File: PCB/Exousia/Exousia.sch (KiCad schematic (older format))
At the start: 74 parts, among them J1 IN/out, J2 I2C buss, J3 in/OUT, Q1 2N7002, Q2 2N7002, Q3 2N7002, U1 AON7410, U2 AON7410, U3 RVSPG, U4 AON7410, U5 AON7410

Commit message: did work
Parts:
- removed J1: IN/out, Connector_PinSocket_2.54mm:PinSocket_1x04_P2.54mm_Vertical, symbol Connector:Conn_01x02_Female
- removed J3: in/OUT, Connector_PinSocket_2.54mm:PinSocket_1x02_P2.54mm_Vertical, symbol Connector:Conn_01x02_Female
- removed TP1: RVSPG, TestPoint:TestPoint_Loop_D2.50mm_Drill1.0mm, symbol Connector:TestPoint
- removed TP2: FRWPG, TestPoint:TestPoint_Loop_D2.50mm_Drill1.0mm, symbol Connector:TestPoint
- added J1: IN/out, Connector_PinSocket_2.54mm:PinSocket_1x04_P2.54mm_Vertical, symbol Connector:Conn_01x04_Female
- added J3: in/OUT, Connector_PinSocket_2.54mm:PinSocket_1x04_P2.54mm_Vertical, symbol Connector:Conn_01x04_Female
- D1, D3: value LED -> FRWPG
- D4: value LED -> RVSPG
- JP1: value SolderJumper_3_Open -> IO-Vselect; footprint Connector_PinSocket_2.54mm:PinSocket_1x03_P2.54mm_Vertical -> Jumper:SolderJumper-3_P1.3mm_Open_RoundedPad1.0x1.5mm_NumberLabels
- JP2: value SolderJumper_3_Open -> Pin_FRWEN / ADP; footprint Connector_PinSocket_2.54mm:PinSocket_1x03_P2.54mm_Vertical -> Jumper:SolderJumper-3_P1.3mm_Open_RoundedPad1.0x1.5mm_NumberLabels
- JP3: value SolderJumper_3_Open -> RVSEN; footprint Connector_PinSocket_2.54mm:PinSocket_1x03_P2.54mm_Vertical -> Jumper:SolderJumper-3_P1.3mm_Open_RoundedPad1.0x1.5mm_NumberLabels
- JP4: value SolderJumper_3_Open -> Pin_FRWEN; footprint Connector_PinSocket_2.54mm:PinSocket_1x03_P2.54mm_Vertical -> Jumper:SolderJumper-3_P1.3mm_Open_RoundedPad1.0x1.5mm_NumberLabels
- L1: footprint (none) -> Inductor_SMD:L_6.3x6.3_H3
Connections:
- net GND: now also J1.1 (Pin_1), J1.2 (Pin_2), J3.1 (Pin_1), J3.2 (Pin_2)
- net at D2.1, R1.2, R2.2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: now also J1.3 (Pin_3), J1.4 (Pin_4)
- net at R24.1, R25.2: now also J3.3 (Pin_3), J3.4 (Pin_4)
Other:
- note added: "change component values for 12A system, \n- inductor\n- mosfets\n- sense resistors\nchange footprint for IC\nmake footprint for inductor"
- note removed: "find foot prints of all passives \n\n"
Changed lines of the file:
@@
 $EndDescr
-$Comp
-L Connector:Conn_01x02_Female J1
-U 1 1 5FC12546
-P 1750 1650
-F 0 "J1" H 1642 1325 50  0000 C CNN
-F 1 "IN/out" H 1642 1416 50  0000 C CNN
-F 2 "Connector_PinSocket_2.54mm:PinSocket_1x04_P2.54mm_Vertical" H 1750 1650 50  0001 C CNN
-F 3 "~" H 1750 1650 50  0001 C CNN
-	1    1750 1650
-	-1   0    0    1
-$EndComp
-$Comp
-L Connector:Conn_01x02_Female J3
-U 1 1 5FC12995
-P 13450 1650
-F 0 "J3" H 13478 1626 50  0000 L CNN
-F 1 "in/OUT" H 13478 1535 50  0000 L CNN
-F 2 "Connector_PinSocket_2.54mm:PinSocket_1x02_P2.54mm_Vertical" H 13450 1650 50  0001 C CNN
-F 3 "~" H 13450 1650 50  0001 C CNN
-	1    13450 1650
-	1    0    0    1
-$EndComp
 $Comp
 L ISL95338:ISL95338 U3
@@
 F 0 "L1" V 7840 2050 50  0000 C CNN
 F 1 "2uH" V 7749 2050 50  0000 C CNN
-F 2 "" H 7650 2050 50  0001 C CNN
+F 2 "Inductor_SMD:L_6.3x6.3_H3" H 7650 2050 50  0001 C CNN
 F 3 "~" H 7650 2050 50  0001 C CNN
 	1    7650 2050
@@
 L power:GND #PWR0105
 U 1 1 5FC5C5A0
-P 2000 1750
-F 0 "#PWR0105" H 2000 1500 50  0001 C CNN
-F 1 "GND" H 2005 1577 50  0000 C CNN
-F 2 "" H 2000 1750 50  0001 C CNN
-F 3 "" H 2000 1750 50  0001 C CNN
-	1    2000 1750
+P 2000 1850
+F 0 "#PWR0105" H 2000 1600 50  0001 C CNN
+F 1 "GND" H 2005 1677 50  0000 C CNN
+F 2 "" H 2000 1850 50  0001 C CNN
+F 3 "" H 2000 1850 50  0001 C CNN
+	1    2000 1850
 	1    0    0    -1
 $EndComp
@@
 Wire Wire Line
 	10000 5100 10000 4950
-$Comp
-L Connector:TestPoint TP2
-U 1 1 5FD06A05
-P 9300 4800
-F 0 "TP2" H 9358 4918 50  0000 L CNN
-F 1 "FRWPG" H 9358 4827 50  0000 L CNN
-F 2 "TestPoint:TestPoint_Loop_D2.50mm_Drill1.0mm" H 9500 4800 50  0001 C CNN
-F 3 "~" H 9500 4800 50  0001 C CNN
-	1    9300 4800
-	1    0    0    -1
-$EndComp
-Wire Wire Line
-	8900 5000 9300 5000
-Wire Wire Line
-	8800 5100 8950 5100
-Wire Wire Line
-	9300 4800 9300 5000
-$Comp
-L Connector:TestPoint TP1
-U 1 1 5FD1FD32
-P 8950 4800
-F 0 "TP1" H 9008 4918 50  0000 L CNN
-F 1 "RVSPG" H 9008 4827 50  0000 L CNN
-F 2 "TestPoint:TestPoint_Loop_D2.50mm_Drill1.0mm" H 9150 4800 50  0001 C CNN
-F 3 "~" H 9150 4800 50  0001 C CNN
-	1    8950 4800
-	1    0    0    -1
-$EndComp
-Wire Wire Line
-	8950 4800 8950 5100
-Connection ~ 8950 5100
-Connection ~ 9300 5000
-Wire Wire Line
-	9300 5000 9650 5000
-Wire Wire Line
-	8950 5100 10000 5100
 Wire Wire Line
 	8900 5000 8900 4550
@@
 L power:GND #PWR0110
 U 1 1 5FD5060D
-P 13200 1700
-F 0 "#PWR0110" H 13200 1450 50  0001 C CNN
-F 1 "GND" H 13205 1527 50  0000 C CNN
-F 2 "" H 13200 1700 50  0001 C CNN
-F 3 "" H 13200 1700 50  0001 C CNN
-	1    13200 1700
-	1    0    0    -1
-$EndComp
-Wire Wire Line
-	13200 1700 13200 1650
+P 13200 1800
+F 0 "#PWR0110" H 13200 1550 50  0001 C CNN
+F 1 "GND" H 13205 1627 50  0000 C CNN
+F 2 "" H 13200 1800 50  0001 C CNN
+F 3 "" H 13200 1800 50  0001 C CNN
+	1    13200 1800
+	1    0    0    -1
+$EndComp
 Wire Wire Line
 	13200 1650 13250 1650
@@
 	3250 2000 3250 2100
 Wire Wire Line
-	1950 1550 2450 1550
+	1950 1550 2000 1550
 Wire Wire Line
 	2450 1550 2450 3900
@@
 P 3350 8800
 F 0 "D1" V 3389 8682 50  0000 R CNN
-F 1 "LED" V 3298 8682 50  0000 R CNN
+F 1 "FRWPG" V 3298 8682 50  0000 R CNN
 F 2 "LED_SMD:LED_1206_3216Metric" H 3350 8800 50  0001 C CNN
 F 3 "~" H 3350 8800 50  0001 C CNN
@@
 P 5050 8800
 F 0 "D3" V 5089 8682 50  0000 R CNN
-F 1 "LED" V 4998 8682 50  0000 R CNN
+F 1 "FRWPG" V 4998 8682 50  0000 R CNN
 F 2 "LED_SMD:LED_1206_3216Metric" H 5050 8800 50  0001 C CNN
 F 3 "~" H 5050 8800 50  0001 C CNN
@@
 P 6550 8800
 F 0 "D4" V 6589 8682 50  0000 R CNN
-F 1 "LED" V 6498 8682 50  0000 R CNN
+F 1 "RVSPG" V 6498 8682 50  0000 R CNN
 F 2 "LED_SMD:LED_1206_3216Metric" H 6550 8800 50  0001 C CNN
 F 3 "~" H 6550 8800 50  0001 C CNN
@@
 P 2400 7900
 F 0 "JP1" H 2400 8105 50  0000 C CNN
-F 1 "SolderJumper_3_Open" H 2400 8014 50  0000 C CNN
-F 2 "Connector_PinSocket_2.54mm:PinSocket_1x03_P2.54mm_Vertical" H 2400 7900 50  0001 C CNN
+F 1 "IO-Vselect" H 2400 8014 50  0000 C CNN
+F 2 "Jumper:SolderJumper-3_P1.3mm_Open_RoundedPad1.0x1.5mm_NumberLabels" H 2400 7900 50  0001 C CNN
 F 3 "~" H 2400 7900 50  0001 C CNN
 	1    2400 7900
@@
 P 4950 4150
 F 0 "JP2" H 4950 4355 50  0000 C CNN
-F 1 "SolderJumper_3_Open" H 4950 4264 50  0000 C CNN
-F 2 "Connector_PinSocket_2.54mm:PinSocket_1x03_P2.54mm_Vertical" H 4950 4150 50  0001 C CNN
+F 1 "Pin_FRWEN / ADP" H 4950 4264 50  0000 C CNN
+F 2 "Jumper:SolderJumper-3_P1.3mm_Open_RoundedPad1.0x1.5mm_NumberLabels" H 4950 4150 50  0001 C CNN
 F 3 "~" H 4950 4150 50  0001 C CNN
 	1    4950 4150
@@
 P 7300 8900
 F 0 "JP3" V 7346 8967 50  0000 L CNN
-F 1 "SolderJumper_3_Open" V 7255 8967 50  0000 L CNN
-F 2 "Connector_PinSocket_2.54mm:PinSocket_1x03_P2.54mm_Vertical" H 7300 8900 50  0001 C CNN
+F 1 "RVSEN" V 7255 8967 50  0000 L CNN
+F 2 "Jumper:SolderJumper-3_P1.3mm_Open_RoundedPad1.0x1.5mm_NumberLabels" H 7300 8900 50  0001 C CNN
 F 3 "~" H 7300 8900 50  0001 C CNN
 	1    7300 8900
@@
 P 8100 8900
 F 0 "JP4" V 8146 8967 50  0000 L CNN
-F 1 "SolderJumper_3_Open" V 8055 8967 50  0000 L CNN
-F 2 "Connector_PinSocket_2.54mm:PinSocket_1x03_P2.54mm_Vertical" H 8100 8900 50  0001 C CNN
+F 1 "Pin_FRWEN" V 8055 8967 50  0000 L CNN
+F 2 "Jumper:SolderJumper-3_P1.3mm_Open_RoundedPad1.0x1.5mm_NumberLabels" H 8100 8900 50  0001 C CNN
 F 3 "~" H 8100 8900 50  0001 C CNN
 	1    8100 8900
@@
 	11250 1550 12150 1550
 Wire Wire Line
-	12550 1550 13250 1550
+	12550 1550 13200 1550
 Wire Wire Line
 	8700 3650 12150 3650
@@
 	4200 3900 2450 3900
 Connection ~ 4200 3900
-Text Notes 1700 10450 0    50   ~ 0
-find foot prints of all passives \n\n
+Text Notes 4150 3150 0    50   ~ 0
+change component values for 12A system, \n- inductor\n- mosfets\n- sense resistors\nchange footprint for IC\nmake footprint for inductor
+$Comp
+L Connector:Conn_01x04_Female J1
+U 1 1 5FE213E3
+P 1750 1650
+F 0 "J1" H 1642 1225 50  0000 C CNN
+F 1 "IN/out" H 1642 1316 50  0000 C CNN
+F 2 "Connector_PinSocket_2.54mm:PinSocket_1x04_P2.54mm_Vertical" H 1750 1650 50  0001 C CNN
+F 3 "~" H 1750 1650 50  0001 C CNN
+	1    1750 1650
+	-1   0    0    1
+$EndComp
+Wire Wire Line
+	1950 1750 2000 1750
+Wire Wire Line
+	2000 1750 2000 1850
+Connection ~ 2000 1750
+Wire Wire Line
+	1950 1450 2000 1450
+Wire Wire Line
+	2000 1450 2000 1550
+Connection ~ 2000 1550
+Wire Wire Line
+	2000 1550 2450 1550
+$Comp
+L Connector:Conn_01x04_Female J3
+U 1 1 5FE9219B
+P 13450 1650
+F 0 "J3" H 13342 1225 50  0000 C CNN
+F 1 "in/OUT" H 13342 1316 50  0000 C CNN
+F 2 "Connector_PinSocket_2.54mm:PinSocket_1x04_P2.54mm_Vertical" H 13450 1650 50  0001 C CNN
+F 3 "~" H 13450 1650 50  0001 C CNN
+	1    13450 1650
+	1    0    0    1
+$EndComp
+Wire Wire Line
+	13200 1750 13250 1750
+Wire Wire Line
+	13200 1650 13200 1750
+Wire Wire Line
+	13200 1750 13200 1800
+Connection ~ 13200 1750
+Wire Wire Line
+	13250 1450 13200 1450
+Wire Wire Line
+	13200 1450 13200 1550
+Connection ~ 13200 1550
+Wire Wire Line
+	13200 1550 13250 1550
+Wire Wire Line
+	8800 5100 10000 5100
+Wire Wire Line
+	8900 5000 9650 5000
 $EndSCHEMATC

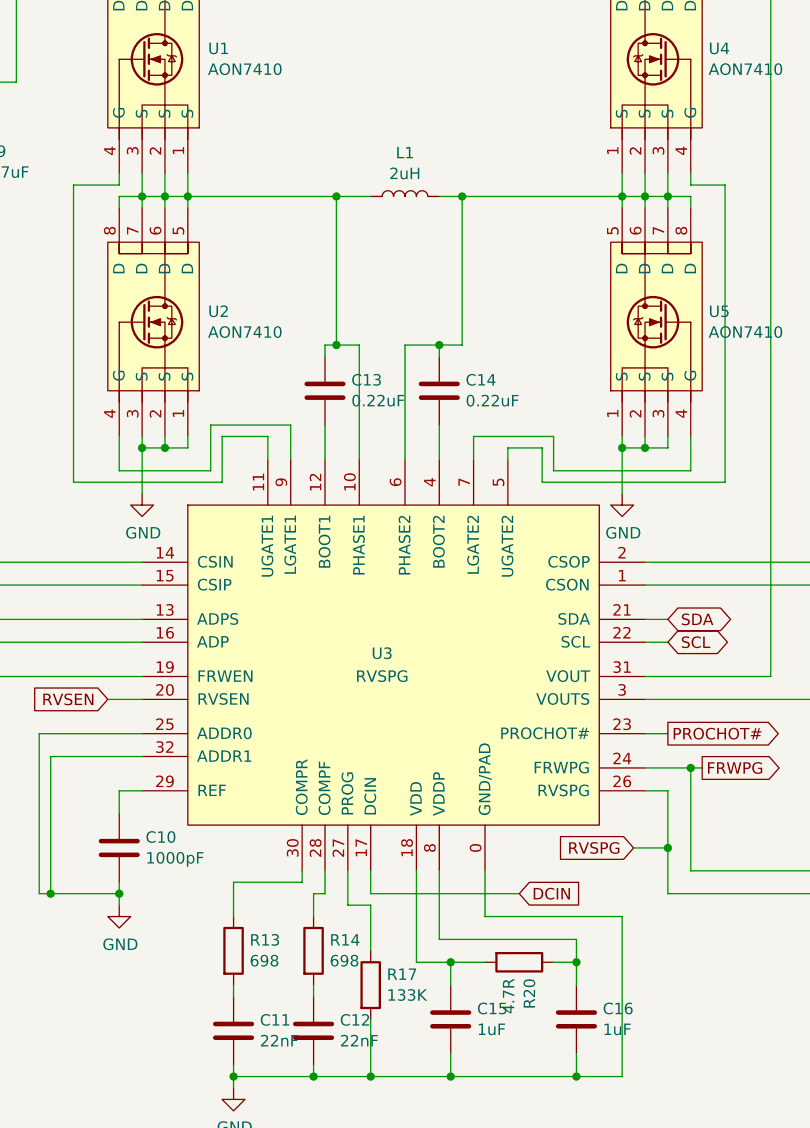
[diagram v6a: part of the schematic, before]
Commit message: updated some footrpints and compoinent valeus for 12A
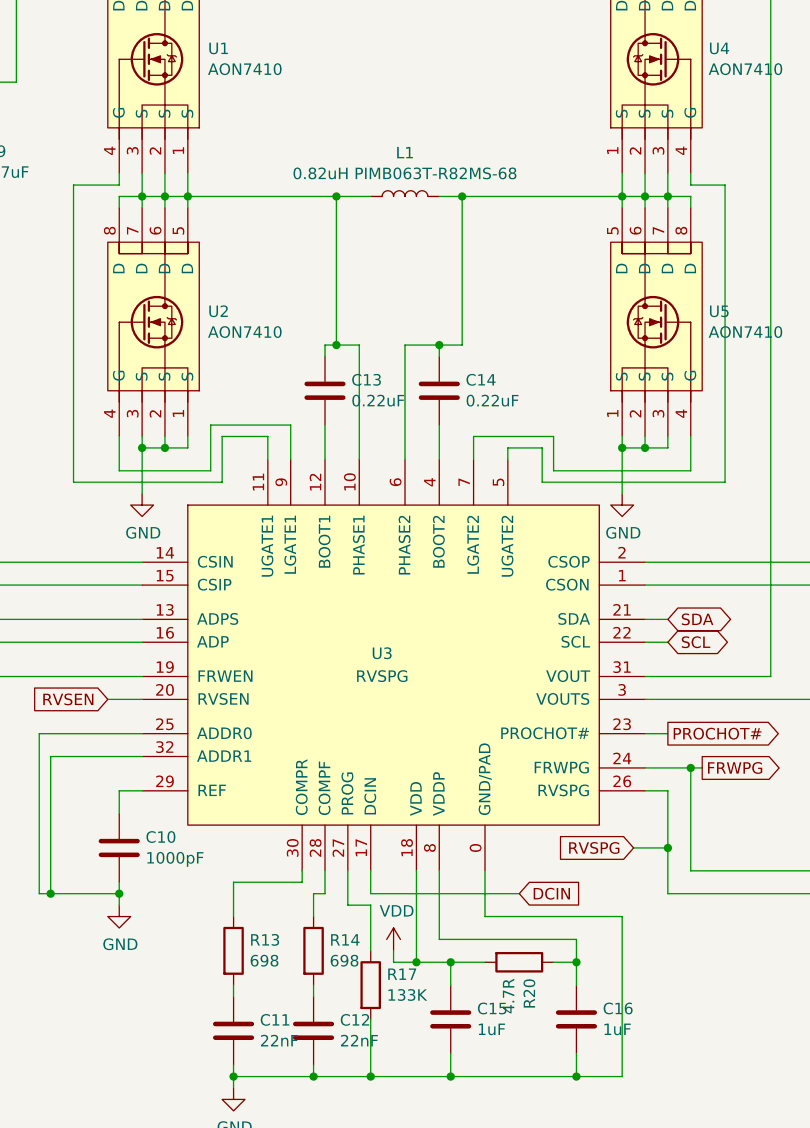
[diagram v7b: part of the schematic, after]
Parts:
- L1: value 2uH -> 0.82uH PIMB063T-R82MS-68; footprint Inductor_SMD:L_6.3x6.3_H3 -> PIMB063T-R82MS-68:PIMB063T-R82MS-68
- U3: footprint Package_DFN_QFN:TQFN-24-1EP_4x4mm_P0.5mm_EP2.8x2.8mm_PullBack -> Package_DFN_QFN:QFN-32-1EP_4x4mm_P0.4mm_EP2.9x2.9mm
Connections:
- net VDD: now also C15.1, R20.2, U3.18 (VDD)
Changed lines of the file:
@@
 F 0 "U3" H 7550 3750 50  0000 C CNN
 F 1 "RVSPG" H 7550 3650 50  0000 C CNN
-F 2 "Package_DFN_QFN:TQFN-24-1EP_4x4mm_P0.5mm_EP2.8x2.8mm_PullBack" H 7550 3900 50  0001 C CNN
+F 2 "Package_DFN_QFN:QFN-32-1EP_4x4mm_P0.4mm_EP2.9x2.9mm" H 7550 3900 50  0001 C CNN
 F 3 "https://www.intersil.com/content/dam/Intersil/documents/isl9/isl95338.pdf" H 7550 3900 50  0001 C CNN
 	1    7550 3900
@@
 P 7650 2050
 F 0 "L1" V 7840 2050 50  0000 C CNN
-F 1 "2uH" V 7749 2050 50  0000 C CNN
-F 2 "Inductor_SMD:L_6.3x6.3_H3" H 7650 2050 50  0001 C CNN
-F 3 "~" H 7650 2050 50  0001 C CNN
+F 1 "0.82uH   PIMB063T-R82MS-68" V 7749 2050 50  0000 C CNN
+F 2 "PIMB063T-R82MS-68:PIMB063T-R82MS-68" H 7650 2050 50  0001 C CNN
+F 3 "http://static6.arrow.com/aropdfconversion/786bc0534771d8612672aefcc8d95d20f5becea1/cyntecpimb063t-r47ms-68spec.pdf" H 7650 2050 50  0001 C CNN
 	1    7650 2050
 	0    -1   -1   0
@@
 Wire Wire Line
 	8900 5000 9650 5000
+$Comp
+L power:VDD #PWR?
+U 1 1 5FFF490C
+P 7600 5350
+F 0 "#PWR?" H 7600 5200 50  0001 C CNN
+F 1 "VDD" H 7615 5523 50  0000 C CNN
+F 2 "" H 7600 5350 50  0001 C CNN
+F 3 "" H 7600 5350 50  0001 C CNN
+	1    7600 5350
+	1    0    0    -1
+$EndComp
+Wire Wire Line
+	7600 5350 7600 5400
+Wire Wire Line
+	7600 5400 7700 5400
+Connection ~ 7700 5400
 $EndSCHEMATC

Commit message: upgraded sens resitors to handle 12A max. and retrouted a bit
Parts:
- R2: value 0.02R -> 0.005R; footprint Resistor_SMD:R_1206_3216Metric -> Resistor_SMD:R_2512_6332Metric
- R24: value 0.01R -> 0.005R; footprint Resistor_SMD:R_1206_3216Metric -> Resistor_SMD:R_2512_6332Metric
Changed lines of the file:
@@
 P 2950 1550
 F 0 "R2" V 2743 1550 50  0000 C CNN
-F 1 "0.02R" V 2834 1550 50  0000 C CNN
-F 2 "Resistor_SMD:R_1206_3216Metric" V 2880 1550 50  0001 C CNN
+F 1 "0.005R" V 2834 1550 50  0000 C CNN
+F 2 "Resistor_SMD:R_2512_6332Metric" V 2880 1550 50  0001 C CNN
 F 3 "~" H 2950 1550 50  0001 C CNN
 	1    2950 1550
@@
 P 12350 1550
 F 0 "R24" V 12143 1550 50  0000 C CNN
-F 1 "0.01R" V 12234 1550 50  0000 C CNN
-F 2 "Resistor_SMD:R_1206_3216Metric" V 12280 1550 50  0001 C CNN
+F 1 "0.005R" V 12234 1550 50  0000 C CNN
+F 2 "Resistor_SMD:R_2512_6332Metric" V 12280 1550 50  0001 C CNN
 F 3 "~" H 12350 1550 50  0001 C CNN
 	1    12350 1550
@@
 	8900 5000 9650 5000
 $Comp
-L power:VDD #PWR?
+L power:VDD #PWR0125
 U 1 1 5FFF490C
 P 7600 5350
-F 0 "#PWR?" H 7600 5200 50  0001 C CNN
+F 0 "#PWR0125" H 7600 5200 50  0001 C CNN
 F 1 "VDD" H 7615 5523 50  0000 C CNN
 F 2 "" H 7600 5350 50  0001 C CNN
